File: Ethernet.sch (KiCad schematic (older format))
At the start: 30 parts, among them J1 Wuerth_7499010121A, U3 DP83848C, Y3 25MHz

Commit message: Finish labelling RAM
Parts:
- gave numbers to parts that had none: 16
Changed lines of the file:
@@
 PFBIN2
 $Comp
-L Device:C C?
+L Device:C C62
 U 1 1 610333B5
 P 4400 6000
-F 0 "C?" H 4515 6046 50  0000 L CNN
+F 0 "C62" H 4515 6046 50  0000 L CNN
 F 1 "10u" H 4515 5955 50  0000 L CNN
 F 2 "" H 4438 5850 50  0001 C CNN
@@
 $EndComp
 $Comp
-L Device:C C?
+L Device:C C63
 U 1 1 61035DAA
 P 4750 6000
-F 0 "C?" H 4865 6046 50  0000 L CNN
+F 0 "C63" H 4865 6046 50  0000 L CNN
 F 1 "100n" H 4865 5955 50  0000 L CNN
 F 2 "" H 4788 5850 50  0001 C CNN
@@
 	4400 5850 4750 5850
 $Comp
-L Device:C C?
+L Device:C C64
 U 1 1 6103CC4A
 P 5200 6000
-F 0 "C?" H 5315 6046 50  0000 L CNN
+F 0 "C64" H 5315 6046 50  0000 L CNN
 F 1 "100n" H 5315 5955 50  0000 L CNN
 F 2 "" H 5238 5850 50  0001 C CNN
@@
 $EndComp
 $Comp
-L Device:C C?
+L Device:C C65
 U 1 1 6103DFDE
 P 5600 6000
-F 0 "C?" H 5715 6046 50  0000 L CNN
+F 0 "C65" H 5715 6046 50  0000 L CNN
 F 1 "100n" H 5715 5955 50  0000 L CNN
 F 2 "" H 5638 5850 50  0001 C CNN
@@
 	5200 6150 5600 6150
 $Comp
-L power:GND #PWR?
+L power:GND #PWR0103
 U 1 1 610482AB
 P 4750 6150
-F 0 "#PWR?" H 4750 5900 50  0001 C CNN
+F 0 "#PWR0103" H 4750 5900 50  0001 C CNN
 F 1 "GND" H 4755 5977 50  0000 C CNN
 F 2 "" H 4750 6150 50  0001 C CNN
@@
 VDD_ETH
 $Comp
-L Device:Ferrite_Bead FB?
+L Device:Ferrite_Bead FB2
 U 1 1 61079906
 P 9100 5650
-F 0 "FB?" V 8826 5650 50  0000 C CNN
+F 0 "FB2" V 8826 5650 50  0000 C CNN
 F 1 "Ferrite_Bead" V 8917 5650 50  0000 C CNN
 F 2 "" V 9030 5650 50  0001 C CNN
@@
 $EndComp
 $Comp
-L Device:C C?
+L Device:C C66
 U 1 1 6107A283
 P 9250 5800
-F 0 "C?" H 9365 5846 50  0000 L CNN
+F 0 "C66" H 9365 5846 50  0000 L CNN
 F 1 "100n" H 9365 5755 50  0000 L CNN
 F 2 "" H 9288 5650 50  0001 C CNN
@@
 $EndComp
 $Comp
-L Device:C C?
+L Device:C C67
 U 1 1 6107BD40
 P 9650 5800
-F 0 "C?" H 9765 5846 50  0000 L CNN
+F 0 "C67" H 9765 5846 50  0000 L CNN
 F 1 "10n" H 9765 5755 50  0000 L CNN
 F 2 "" H 9688 5650 50  0001 C CNN
@@
 	8300 1200 8300 1050
 $Comp
-L power:GND #PWR?
+L power:GND #PWR0104
 U 1 1 610AA7DF
 P 9250 5950
-F 0 "#PWR?" H 9250 5700 50  0001 C CNN
+F 0 "#PWR0104" H 9250 5700 50  0001 C CNN
 F 1 "GND" H 9255 5777 50  0000 C CNN
 F 2 "" H 9250 5950 50  0001 C CNN
@@
 $EndComp
 $Comp
-L power:GND #PWR?
+L power:GND #PWR0105
 U 1 1 610AAE4B
 P 9650 5950
-F 0 "#PWR?" H 9650 5700 50  0001 C CNN
+F 0 "#PWR0105" H 9650 5700 50  0001 C CNN
 F 1 "GND" H 9655 5777 50  0000 C CNN
 F 2 "" H 9650 5950 50  0001 C CNN
@@
 VDD_ETH
 $Comp
-L Device:C C?
+L Device:C C57
 U 1 1 610C217C
 P 1500 5550
-F 0 "C?" H 1615 5596 50  0000 L CNN
+F 0 "C57" H 1615 5596 50  0000 L CNN
 F 1 "10u" H 1615 5505 50  0000 L CNN
 F 2 "" H 1538 5400 50  0001 C CNN
@@
 $EndComp
 $Comp
-L Device:C C?
+L Device:C C58
 U 1 1 610C2831
 P 1850 5550
-F 0 "C?" H 1965 5596 50  0000 L CNN
+F 0 "C58" H 1965 5596 50  0000 L CNN
 F 1 "100n" H 1965 5505 50  0000 L CNN
 F 2 "" H 1888 5400 50  0001 C CNN
@@
 $EndComp
 $Comp
-L Device:C C?
+L Device:C C59
 U 1 1 610C63B4
 P 2200 5550
-F 0 "C?" H 2315 5596 50  0000 L CNN
+F 0 "C59" H 2315 5596 50  0000 L CNN
 F 1 "100n" H 2315 5505 50  0000 L CNN
 F 2 "" H 2238 5400 50  0001 C CNN
@@
 $EndComp
 $Comp
-L Device:C C?
+L Device:C C60
 U 1 1 610CADB5
 P 2750 5550
-F 0 "C?" H 2865 5596 50  0000 L CNN
+F 0 "C60" H 2865 5596 50  0000 L CNN
 F 1 "100n" H 2865 5505 50  0000 L CNN
 F 2 "" H 2788 5400 50  0001 C CNN
@@
 $EndComp
 $Comp
-L Device:C C?
+L Device:C C61
 U 1 1 610D018C
 P 3200 5550
-F 0 "C?" H 3315 5596 50  0000 L CNN
+F 0 "C61" H 3315 5596 50  0000 L CNN
 F 1 "10u" H 3315 5505 50  0000 L CNN
 F 2 "" H 3238 5400 50  0001 C CNN
@@
 	1850 5400 2200 5400
 $Comp
-L power:GND #PWR?
+L power:GND #PWR0106
 U 1 1 610D6B43
 P 1850 5700
-F 0 "#PWR?" H 1850 5450 50  0001 C CNN
+F 0 "#PWR0106" H 1850 5450 50  0001 C CNN
 F 1 "GND" H 1855 5527 50  0000 C CNN
 F 2 "" H 1850 5700 50  0001 C CNN
@@
 	2950 5400 3200 5400
 $Comp
-L power:GND #PWR?
+L power:GND #PWR0107
 U 1 1 610DF320
 P 2950 5700
-F 0 "#PWR?" H 2950 5450 50  0001 C CNN
+F 0 "#PWR0107" H 2950 5450 50  0001 C CNN
 F 1 "GND" H 2955 5527 50  0000 C CNN
 F 2 "" H 2950 5700 50  0001 C CNN
@@
 LED_GREEN
 $Comp
-L Device:R R?
+L Device:R R7
 U 1 1 6113745C
 P 2100 4400
-F 0 "R?" H 2170 4446 50  0000 L CNN
+F 0 "R7" H 2170 4446 50  0000 L CNN
 F 1 "470" H 2170 4355 50  0000 L CNN
 F 2 "" V 2030 4400 50  0001 C CNN
@@
 $EndComp
 $Comp
-L power:GND #PWR?
+L power:GND #PWR0108
 U 1 1 6114D2DD
 P 2850 1400
-F 0 "#PWR?" H 2850 1150 50  0001 C CNN
+F 0 "#PWR0108" H 2850 1150 50  0001 C CNN
 F 1 "GND" H 2855 1227 50  0000 C CNN
 F 2 "" H 2850 1400 50  0001 C CNN
@@
 	2300 1400 2300 1550
 $Comp
-L Device:R R?
+L Device:R R16
 U 1 1 611611C3
 P 2850 4000
-F 0 "R?" H 2920 4046 50  0000 L CNN
+F 0 "R16" H 2920 4046 50  0000 L CNN
 F 1 "220" H 2920 3955 50  0000 L CNN
 F 2 "" V 2780 4000 50  0001 C CNN
@@
 $EndComp
 $Comp
-L Device:R R?
+L Device:R R17
 U 1 1 611611C9
 P 2850 4400
-F 0 "R?" H 2920 4446 50  0000 L CNN
+F 0 "R17" H 2920 4446 50  0000 L CNN
 F 1 "470" H 2920 4355 50  0000 L CNN
 F 2 "" V 2780 4400 50  0001 C CNN
@@
 	2850 4250 2850 4200
 $Comp
-L power:GND #PWR?
+L power:GND #PWR0109
 U 1 1 6116AE16
 P 2100 4550
-F 0 "#PWR?" H 2100 4300 50  0001 C CNN
+F 0 "#PWR0109" H 2100 4300 50  0001 C CNN
 F 1 "GND" H 2105 4377 50  0000 C CNN
 F 2 "" H 2100 4550 50  0001 C CNN
@@
 $EndComp
 $Comp
-L power:GND #PWR?
+L power:GND #PWR0110
 U 1 1 6116B683
 P 2850 4550
-F 0 "#PWR?" H 2850 4300 50  0001 C CNN
+F 0 "#PWR0110" H 2850 4300 50  0001 C CNN
 F 1 "GND" H 2855 4377 50  0000 C CNN
 F 2 "" H 2850 4550 50  0001 C CNN
@@
 LED Resistors
 $Comp
-L Device:R R?
+L Device:R R6
 U 1 1 61136A3F
 P 2100 4000
-F 0 "R?" H 2170 4046 50  0000 L CNN
+F 0 "R6" H 2170 4046 50  0000 L CNN
 F 1 "220" H 2170 3955 50  0000 L CNN
 F 2 "" V 2030 4000 50  0001 C CNN

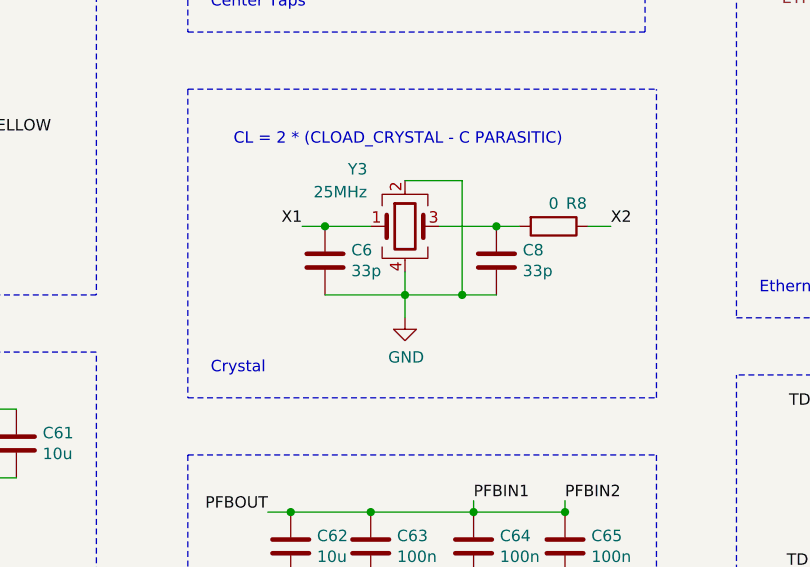
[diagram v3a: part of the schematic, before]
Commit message: Finish DDR schematic
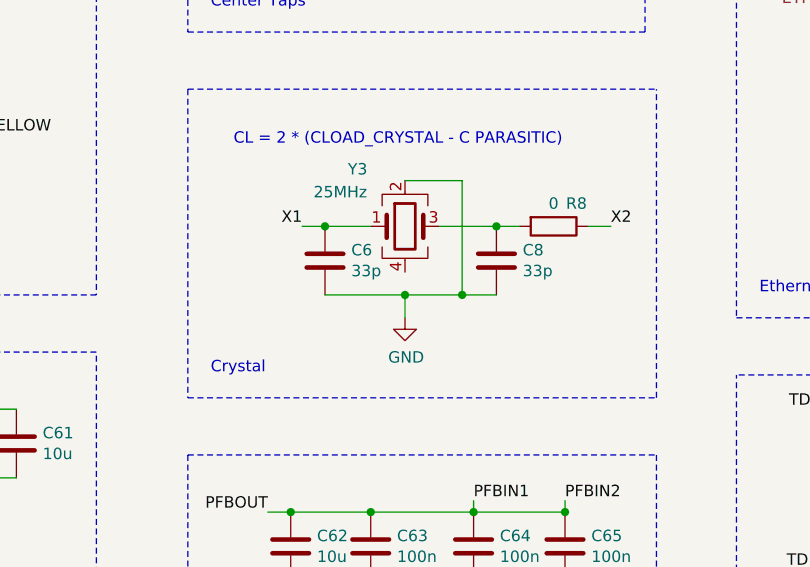
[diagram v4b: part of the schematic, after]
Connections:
- net GND: no longer Y3.4
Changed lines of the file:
@@
 Wire Wire Line
 	5150 4900 4900 4900
-Wire Wire Line
-	4900 4900 4900 4800
 $Comp
 L power:GND #PWR017

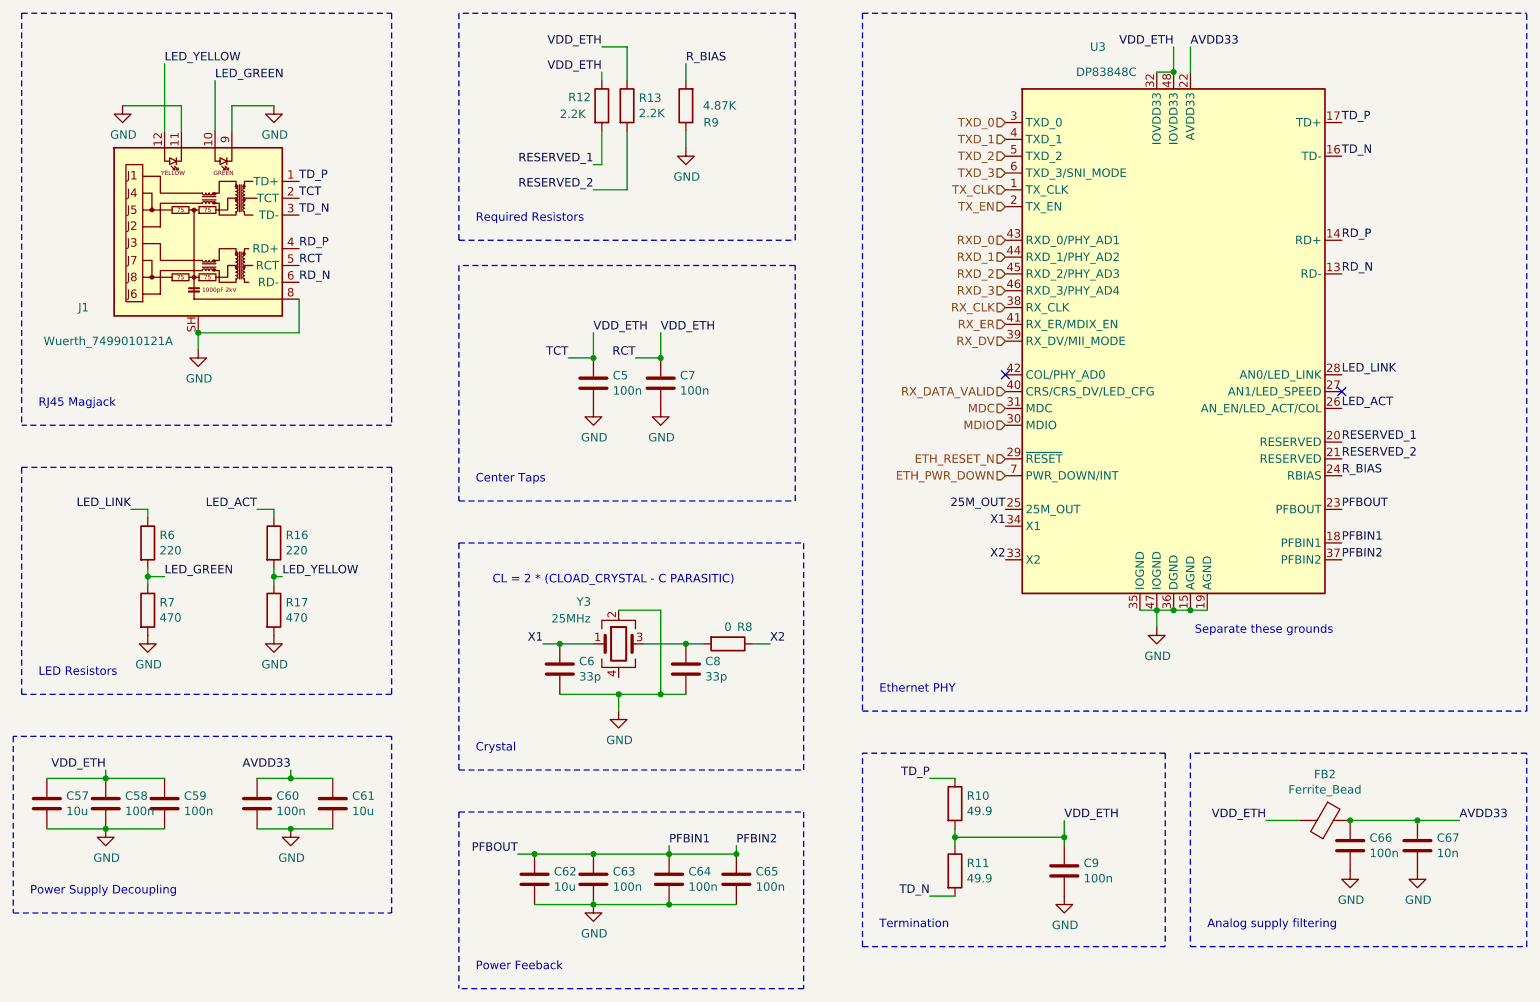
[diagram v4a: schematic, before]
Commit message: Add DC barrel connector for alternate power supply
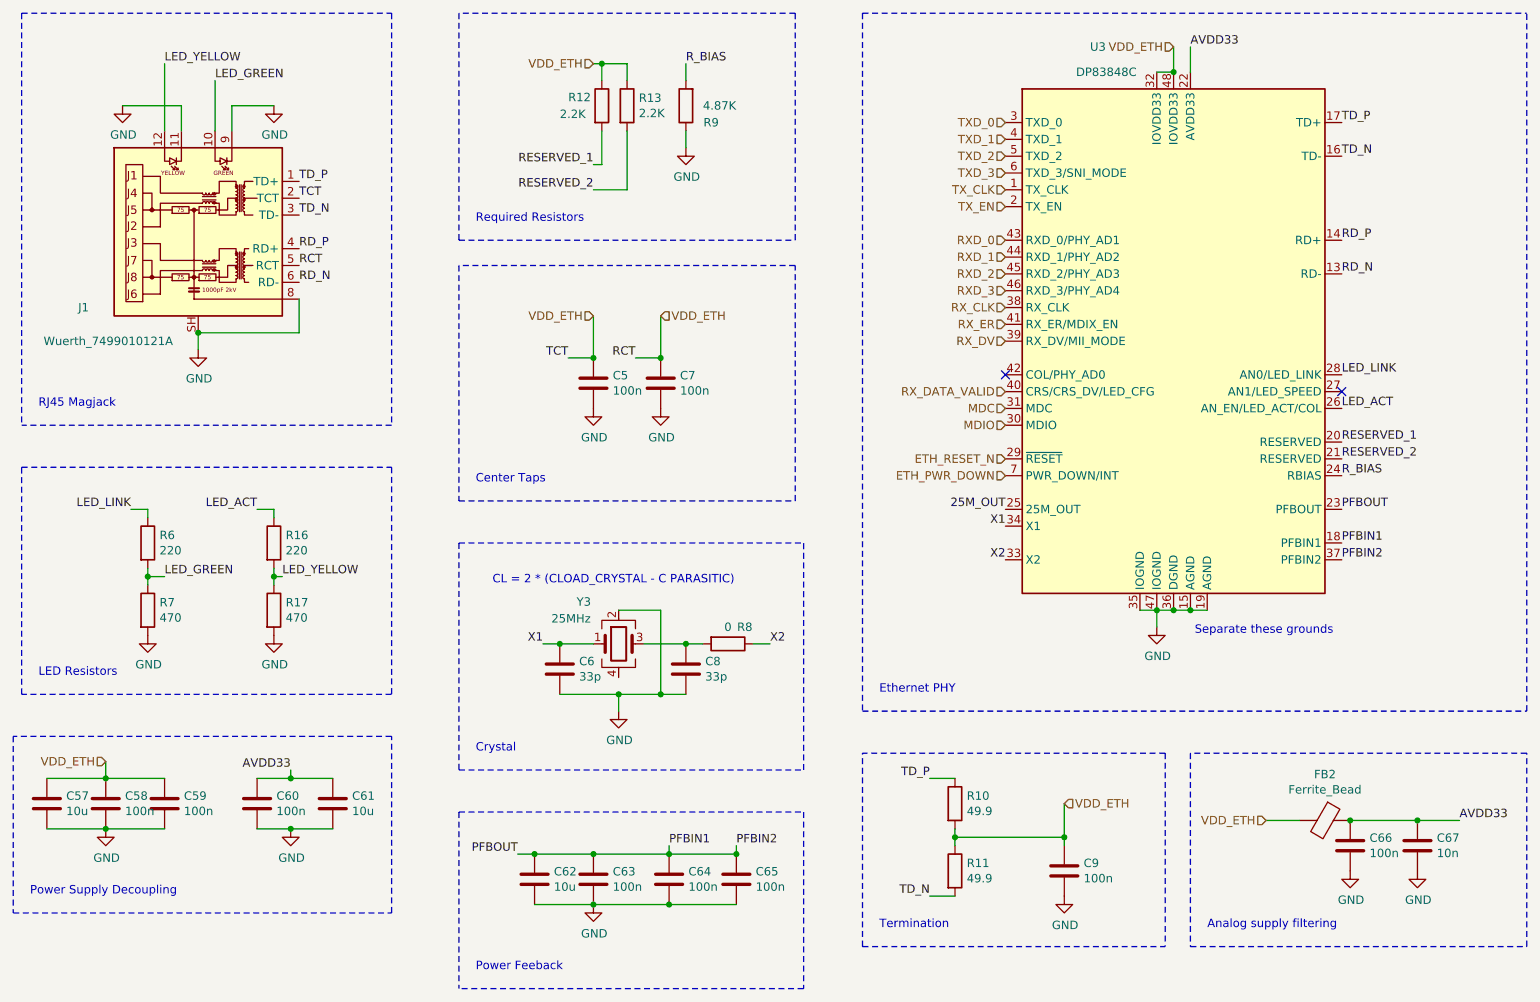
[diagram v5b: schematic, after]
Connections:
- net RCT renamed VDD_ETH
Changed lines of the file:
@@
 	1    0    0    -1
 $EndComp
-Wire Wire Line
-	4750 2900 4750 2750
 Connection ~ 4750 2900
-Wire Wire Line
-	5150 2900 5150 2750
 Connection ~ 5150 2900
 $Comp
@@
 Wire Wire Line
 	7550 5800 7550 5750
-Text Label 7550 5650 0    50   ~ 0
-VDD_ETH
-Wire Wire Line
-	7550 5650 7550 5750
 Connection ~ 7550 5750
 $Comp
@@
 Wire Wire Line
 	6900 5750 6900 5800
-Text Label 5150 2750 0    50   ~ 0
-VDD_ETH
-Text Label 4750 2750 0    50   ~ 0
-VDD_ETH
 $Comp
 L power:GND #PWR013
@@
 	3000 2750 3000 2550
 Connection ~ 2400 2750
-Text Label 4800 1050 2    50   ~ 0
-VDD_ETH
-Text Label 4800 1200 2    50   ~ 0
-VDD_ETH
-Wire Wire Line
-	4800 1200 4800 1250
 Text Label 7200 3800 2    50   ~ 0
 25M_OUT
@@
 Text HLabel 7200 3100 0    50   Input ~ 0
 RX_DATA_VALID
-Text Label 8750 5650 2    50   ~ 0
-VDD_ETH
 $Comp
 L Device:Ferrite_Bead FB2
@@
 Text Label 8300 1050 0    50   ~ 0
 AVDD33
-Text Label 8200 1050 2    50   ~ 0
-VDD_ETH
 Wire Wire Line
 	8200 1050 8200 1200
@@
 Text Label 2950 5350 2    50   ~ 0
 AVDD33
-Text Label 1850 5350 2    50   ~ 0
-VDD_ETH
 $Comp
 L Device:C C57
@@
 $EndComp
 Wire Wire Line
-	1850 5400 1850 5350
-Wire Wire Line
 	2950 5350 2950 5400
 Connection ~ 2950 5400
@@
 	4950 1900 4950 1550
 Wire Wire Line
-	4800 1050 4950 1050
-Wire Wire Line
-	4950 1050 4950 1250
-Wire Wire Line
 	4750 1900 4950 1900
 Text Label 9200 3400 0    50   ~ 0
@@
 Wire Notes Line
 	6350 850  10300 850
+Text HLabel 8750 5650 0    50   Input ~ 0
+VDD_ETH
+Text HLabel 8200 1050 0    50   Input ~ 0
+VDD_ETH
+Text HLabel 4750 1150 0    50   Input ~ 0
+VDD_ETH
+Text HLabel 4750 2650 0    50   Input ~ 0
+VDD_ETH
+Text HLabel 5150 2650 2    50   Input ~ 0
+VDD_ETH
+Text HLabel 1850 5300 0    50   Input ~ 0
+VDD_ETH
+Wire Wire Line
+	1850 5300 1850 5400
+Wire Wire Line
+	5150 2650 5150 2900
+Wire Wire Line
+	4750 2650 4750 2900
+Wire Wire Line
+	4750 1150 4800 1150
+Wire Wire Line
+	4800 1150 4800 1250
+Wire Wire Line
+	4800 1150 4950 1150
+Wire Wire Line
+	4950 1150 4950 1250
+Connection ~ 4800 1150
+Text HLabel 7550 5550 2    50   Input ~ 0
+VDD_ETH
+Wire Wire Line
+	7550 5550 7550 5750
 $EndSCHEMATC

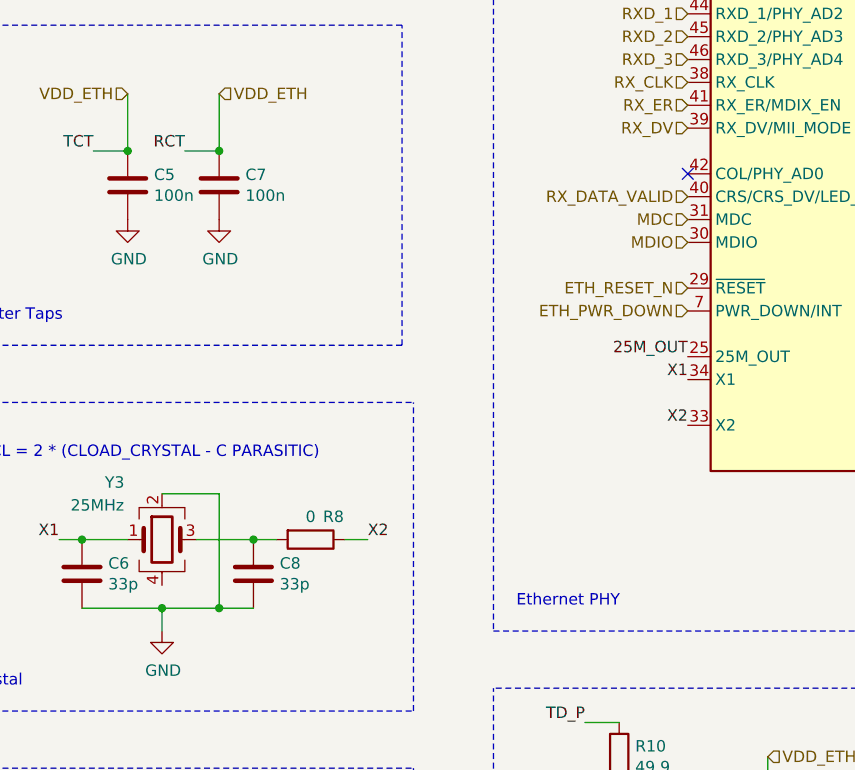
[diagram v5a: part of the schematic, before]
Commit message: Start crossing off ERC. Add generated BOM
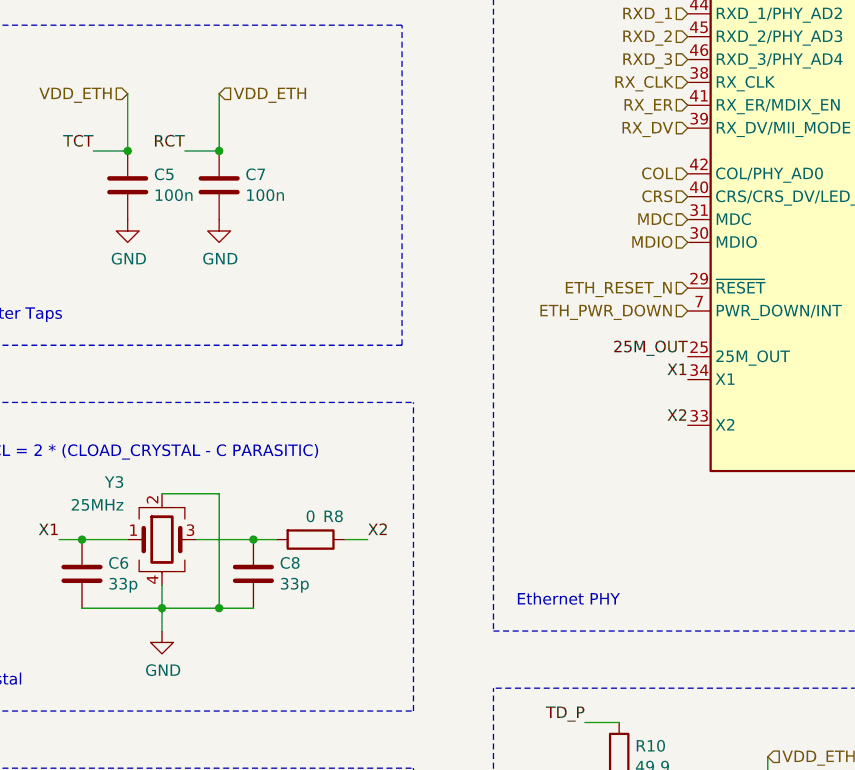
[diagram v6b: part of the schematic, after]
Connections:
- net GND: now also Y3.4
- net COL: now reaches U3.42 (COL/PHY_AD0)
- net RX_DATA_VALID renamed CRS
- no-connect marks 2 -> 1
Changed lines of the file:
@@
 $Descr A4 11693 8268
 encoding utf-8
-Sheet 5 6
+Sheet 6 6
 Title ""
 Date ""
@@
 	1    0    0    -1
 $EndComp
-NoConn ~ 7200 3000
 Text HLabel 7200 3100 0    50   Input ~ 0
-RX_DATA_VALID
+CRS
 $Comp
 L Device:Ferrite_Bead FB2
@@
 Wire Wire Line
 	7550 5550 7550 5750
+Text HLabel 7200 3000 0    50   Input ~ 0
+COL
+Wire Wire Line
+	4900 4800 4900 4900
 $EndSCHEMATC

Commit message: Complete schematic rough draft
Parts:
- added R36: DNP, symbol Device:R
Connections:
- net GND: now also R36.2
- net 25M_OUT: no longer names the net of U3.25 (25M_OUT)
- net 25M_OUT: now also R36.1
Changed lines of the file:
@@
 	3000 2750 3000 2550
 Connection ~ 2400 2750
-Text Label 7200 3800 2    50   ~ 0
-25M_OUT
 Text Label 9200 4000 0    50   ~ 0
 PFBIN1
@@
 Wire Wire Line
 	4900 4800 4900 4900
+Wire Wire Line
+	7200 3800 6800 3800
+Wire Wire Line
+	6800 3800 6800 3900
+$Comp
+L Device:R R36
+U 1 1 6118CB6B
+P 6800 4050
+F 0 "R36" H 6870 4096 50  0000 L CNN
+F 1 "DNP" H 6870 4005 50  0000 L CNN
+F 2 "" V 6730 4050 50  0001 C CNN
+F 3 "~" H 6800 4050 50  0001 C CNN
+	1    6800 4050
+	1    0    0    -1
+$EndComp
+$Comp
+L power:GND #PWR039
+U 1 1 6118D23D
+P 6800 4200
+F 0 "#PWR039" H 6800 3950 50  0001 C CNN
+F 1 "GND" H 6805 4027 50  0000 C CNN
+F 2 "" H 6800 4200 50  0001 C CNN
+F 3 "" H 6800 4200 50  0001 C CNN
+	1    6800 4200
+	1    0    0    -1
+$EndComp
+$Comp
+L power:PWR_FLAG #FLG0102
+U 1 1 611AF76A
+P 9650 5650
+F 0 "#FLG0102" H 9650 5725 50  0001 C CNN
+F 1 "PWR_FLAG" H 9650 5823 50  0000 C CNN
+F 2 "" H 9650 5650 50  0001 C CNN
+F 3 "~" H 9650 5650 50  0001 C CNN
+	1    9650 5650
+	1    0    0    -1
+$EndComp
 $EndSCHEMATC
